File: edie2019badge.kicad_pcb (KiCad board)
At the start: 2 copper layers, 90 x 95.7 mm, 82 parts, among them CN2 2x2, CN3 2x2, CN4 2x2, CN5 1x6_vertical_sm, IC1 ESP-32-WROOM, IC2 XC6206P332MR, IC4 DW01, SW1 switch_3x4, SW2 switch_3x4, SW3 switch_3x4, T1 AO3401, T2 AO3400, T3 FS8205A

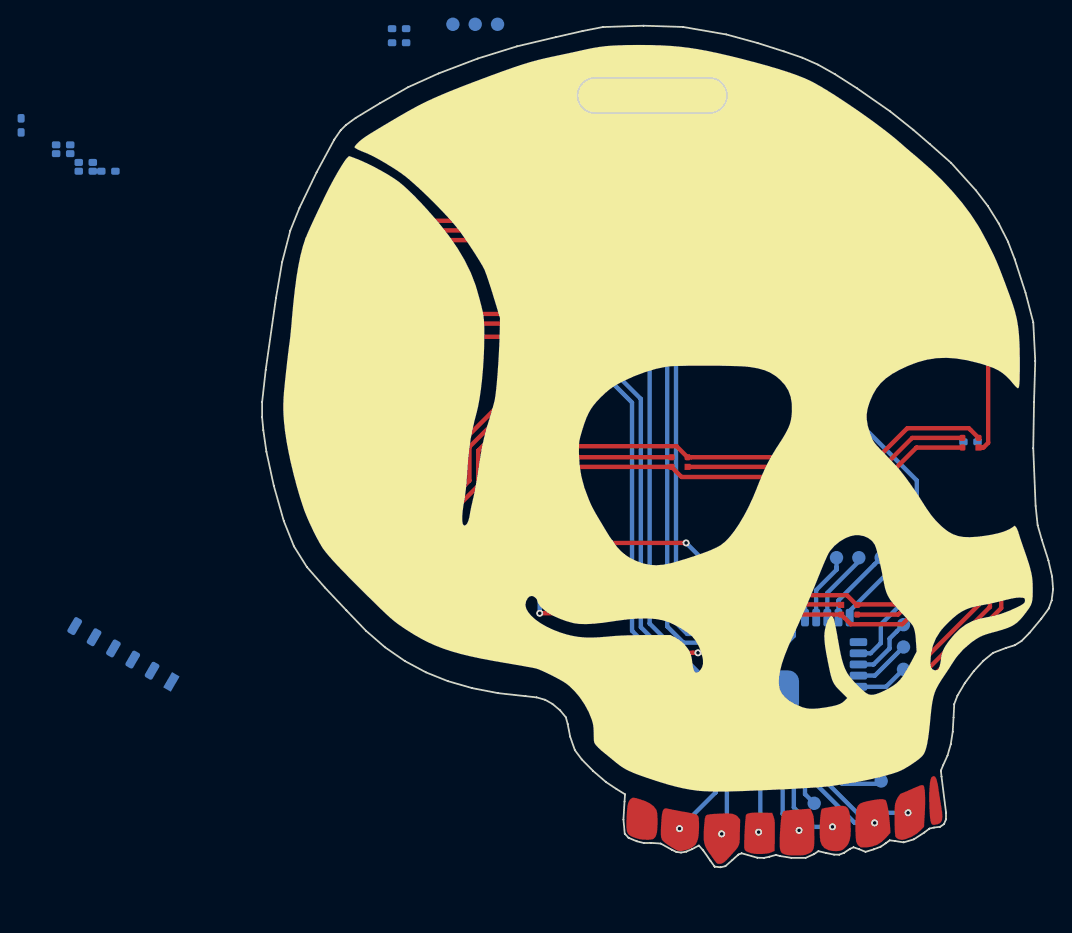
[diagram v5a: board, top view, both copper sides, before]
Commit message: charger layout partially done
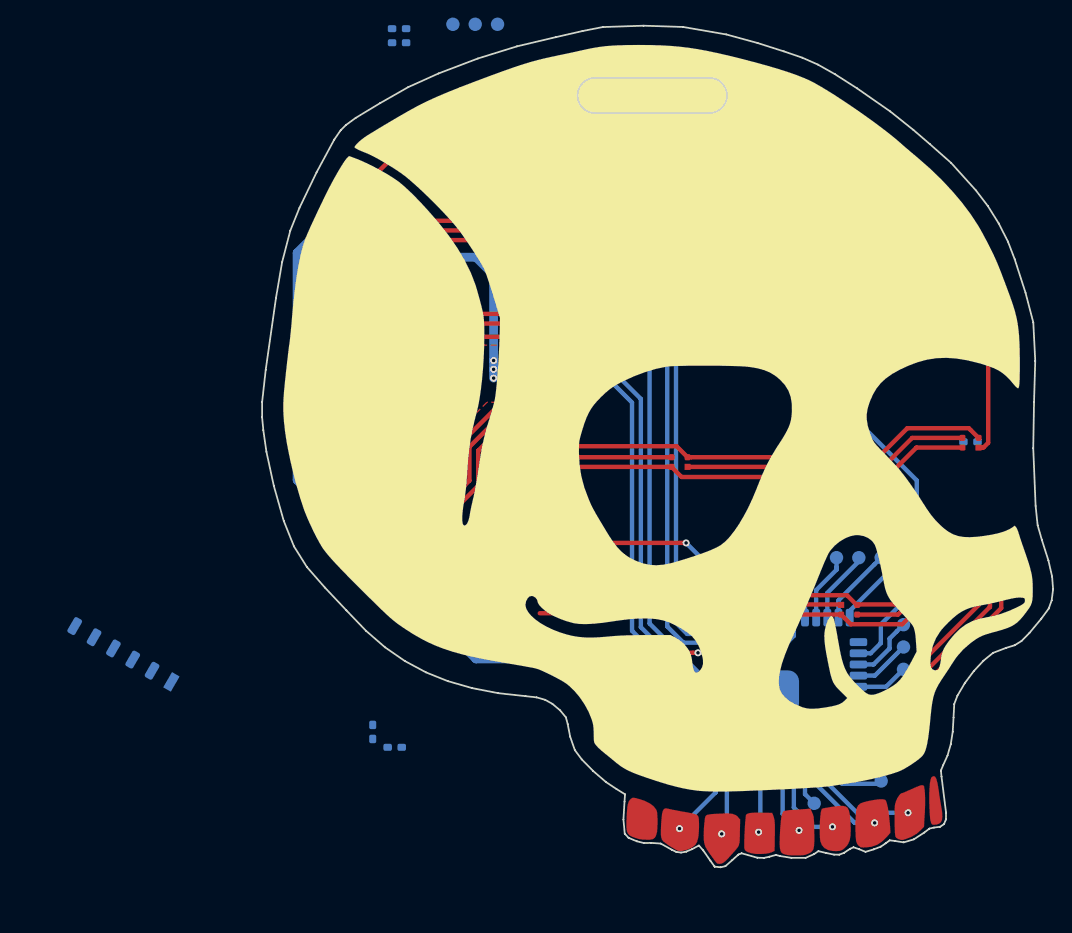
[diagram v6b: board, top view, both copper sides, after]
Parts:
- added BAT1: Battery, PCB:battery_wires, B.Cu at (58.0, 78.5)
- added IC3: TP4056, SOP:SOP-8, B.Cu at (61.5, 88.5)
- moved R5 51.1 mm to (67.0, 88.0)
- moved R9 50.8 mm to (67.0, 86.5)
- moved C9 49.6 mm to (56.0, 90.5), turned to 180 degrees
- moved R10 44.1 mm to (67.0, 85.0)
- moved R8 41.9 mm to (61.5, 84.5)
- moved T2 40.8 mm to (53.0, 76.5), turned to 0 degrees
- moved R4 39.0 mm to (56.0, 88.0)
- moved R3 38.9 mm to (53.0, 79.5)
- moved T1 38.9 mm to (53.0, 82.5)
- moved R7 38.4 mm to (61.5, 128.2)
- moved R6 34.9 mm to (59.0, 126.5), turned to 270 degrees
- moved IC2 31.5 mm to (57.0, 95.0), turned to 270 degrees
- moved R12 29.1 mm to (67.0, 76.5), turned to 0 degrees
- moved C1 27.5 mm to (60.0, 95.0), turned to 90 degrees
- moved T3 26.3 mm to (63.5, 72.5), turned to 0 degrees
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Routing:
- net /LED strip/+V_LEDs: track 388.3 -> 503.8 mm, vias 0 -> 6
- net GND: track 417.4 -> 456.1 mm, vias 0 -> 8
- net VCC: track 5.93 -> 32.1 mm
- net +5V_USB: track 0.00 -> 23.4 mm
- net +3V3: track 25.2 -> 39.2 mm, vias 2 -> 3
- net Net-(IC3-Pad1): track 0.00 -> 7.60 mm
- net Net-(IC4-Pad1): track 0.00 -> 5.49 mm
- net Net-(BAT1-Pad2): track 8.70 -> 13.9 mm
- net Net-(IC4-Pad3): track 9.30 -> 5.49 mm
- net /LED strip/LED_strip_enable: track 38.0 -> 35.6 mm, vias 2 -> 1
- net Net-(IC3-Pad2): track 0.00 -> 2.01 mm
- net /esp32/battery_charging: track 54.4 -> 56.4 mm
- net Net-(IC4-Pad2): track 2.00 -> 3.67 mm
- net Net-(C10-Pad1): track 1.92 -> 3.42 mm
- net Net-(R3-Pad2): track 5.01 -> 4.19 mm
- added copper zone on F.Cu, net GND

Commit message: added USB connector
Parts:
- added CN1: USB-Micro, USB:micro_usb, B.Cu at (64.5, 57.5)
- moved R2 25.7 mm to (77.5, 67.0), turned to 180 degrees
- moved R1 23.2 mm to (77.5, 65.4), turned to 0 degrees
- moved R7 2.02 mm to (60.5, 126.5), turned to 270 degrees
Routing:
- net /LED strip/LED_strip_enable: track 35.6 -> 62.5 mm
- net +3V3: track 39.2 -> 30.6 mm, vias 3 -> 2
- net /LED strip/+V_LEDs: track 503.8 -> 505.5 mm
- net Net-(IC1-Pad25): track 69.8 -> 70.6 mm

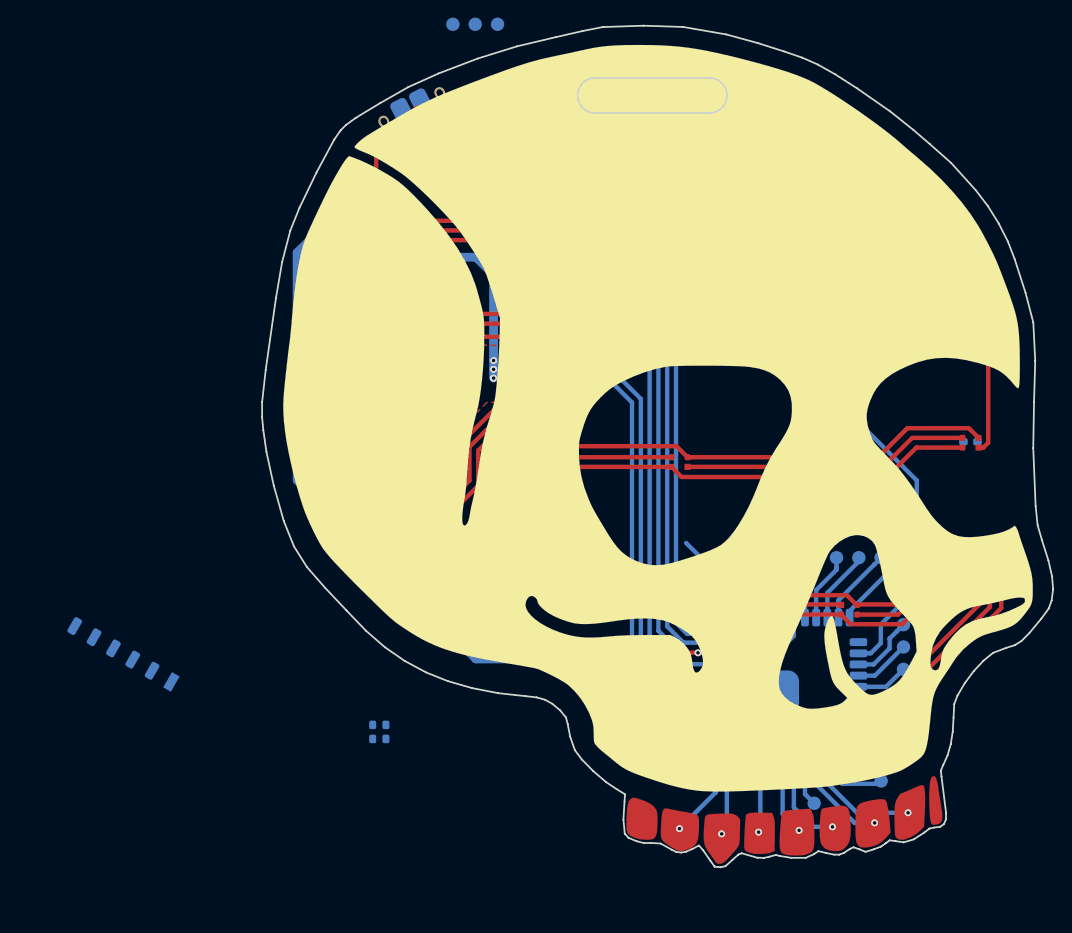
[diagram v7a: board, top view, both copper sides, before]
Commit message: almost all nets complete in layout
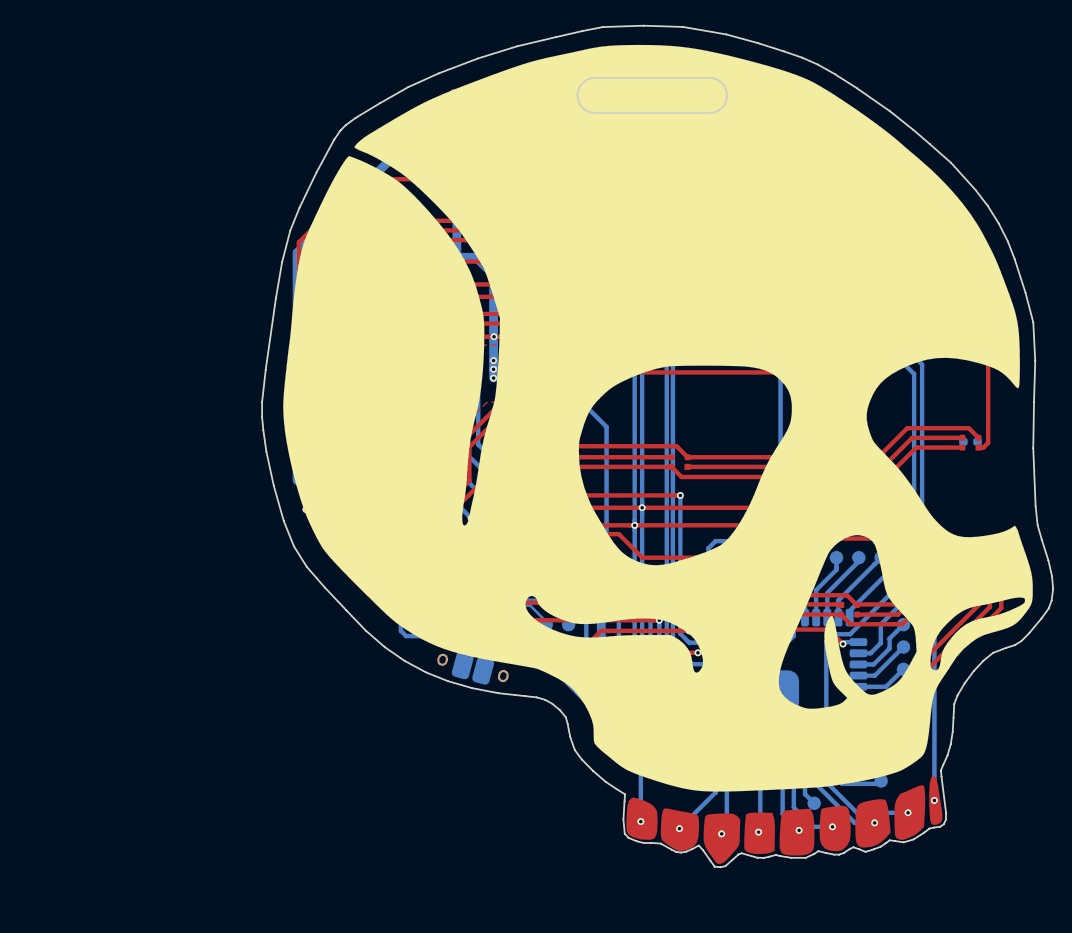
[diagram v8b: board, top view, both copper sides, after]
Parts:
- removed CN5: 1x6_vertical_sm, pin_headers:1x6_vertical_sm
- added C11: C, SMT:0603, B.Cu at (79.0, 110.0)
- added C12: C, SMT:0603, B.Cu at (66.4, 111.6)
- added IC5: FT230XS, SSOP:SSOP-16, B.Cu at (72.5, 110.5)
- added TP20: test_point, PCB:test_point, B.Cu at (63.5, 114.3)
- added TP21: test_point, PCB:test_point, B.Cu at (66.0, 109.2)
- added TP22: test_point, PCB:test_point, B.Cu at (78.7, 114.3)
- added TP23: test_point, PCB:test_point, B.Cu at (81.3, 114.3)
- added TP24: test_point, PCB:test_point, B.Cu at (66.0, 106.7)
- added TP25: test_point, PCB:test_point, B.Cu at (76.2, 114.3)
- moved R6 66.9 mm to (66.0, 60.0), turned to 30 degrees
- moved R7 65.3 mm to (67.0, 61.5), turned to 30 degrees
- moved CN1 59.9 mm to (71.0, 117.0), turned to 165 degrees
- moved R1 51.1 mm to (79.0, 116.5)
- moved R2 49.8 mm to (82.5, 116.5), turned to 0 degrees
- moved TP19 12.2 mm to (66.0, 55.9)
- moved TP18 10.3 mm to (71.1, 55.9)
- moved TP1 10.1 mm to (68.6, 55.9)
- moved SW3 1.30 mm to (120.0, 74.1), turned to 180 degrees
- turned C7 to 180 degrees
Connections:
- CN1 pad 0: GND -> Net-(CN1-Pad0)
- CN1 pad 2: Net-(CN1-Pad2) -> /USB interface/USBN
- CN1 pad 3: Net-(CN1-Pad3) -> /USB interface/USBP
- CN1 pad 4: Net-(CN1-Pad4) -> GND
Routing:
- net GND: track 456.1 -> 773.9 mm, vias 8 -> 24
- net +3V3: track 30.6 -> 187.2 mm, vias 2 -> 6
- net /esp32/SCL: track 8.70 -> 147.0 mm, vias 1 -> 4
- net /esp32/SDA: track 7.84 -> 142.9 mm, vias 1 -> 5
- net +5V_USB: track 23.4 -> 100.4 mm
- net Net-(IC1-Pad23): track 0.00 -> 66.2 mm, vias 0 -> 1
- net /LED strip/+V_LEDs: track 505.5 -> 548.5 mm, vias 6 -> 7
- net /LED strip/LED_strip_enable: track 62.5 -> 101.7 mm, vias 1 -> 2
- net Net-(IC1-Pad25): track 70.6 -> 102.2 mm
- net /USB interface/TX: track 74.2 -> 44.1 mm, vias 0 -> 2
- net /USB interface/RX: track 73.9 -> 43.8 mm, vias 0 -> 2
- net Net-(C12-Pad1): track 0.00 -> 28.2 mm
- net /esp32/battery_charging: track 56.4 -> 83.9 mm, vias 1 -> 2
- net /USB interface/USB_power: track 52.6 -> 27.5 mm, vias 1 -> 2
- net /USB interface/USBP: track 0.00 -> 10.7 mm
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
